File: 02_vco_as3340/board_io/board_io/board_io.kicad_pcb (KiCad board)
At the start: 2 copper layers, 48.8 x 55 mm, 9 parts, among them J1 Conn_02x05_Odd_Even, J2 Conn_02x04_Odd_Even, SW2 SW_SPDT

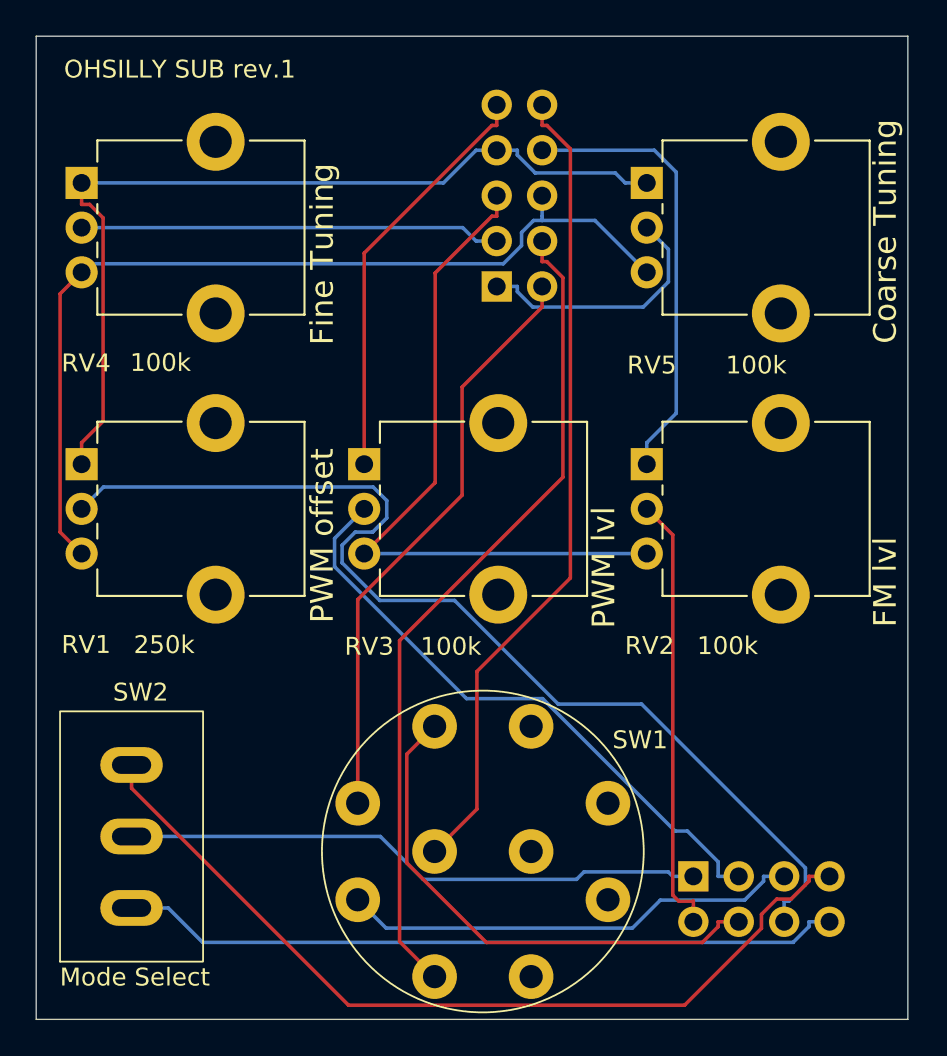
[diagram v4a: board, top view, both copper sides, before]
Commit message: fixed potentiometer direction
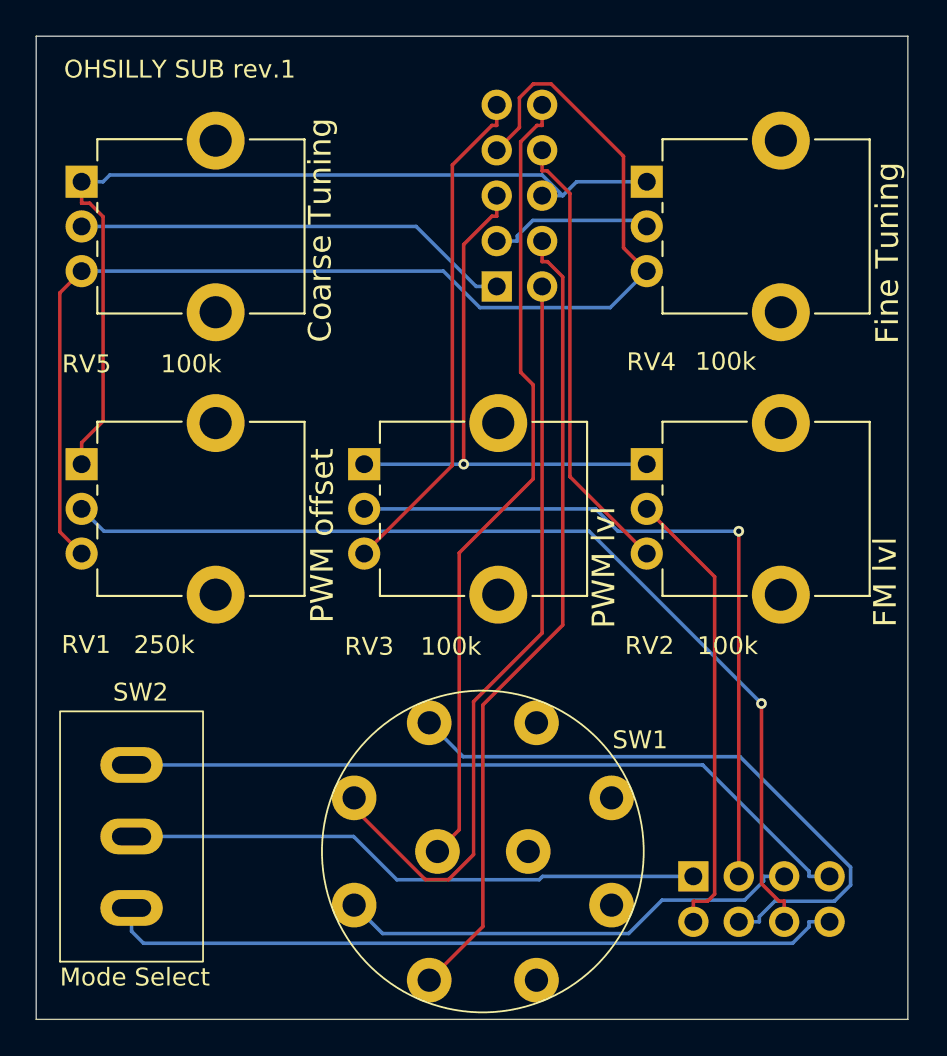
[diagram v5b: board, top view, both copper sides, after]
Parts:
- moved RV4 31.6 mm to (48.8, 26.5)
- moved RV5 31.6 mm to (17.2, 26.5)
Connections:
- RV1 pad 1: +12V -> -12V
- RV1 pad 3: -12V -> +12V
- RV2 pad 1: FM CV Hot -> GND
- RV2 pad 3: GND -> FM CV Hot
- RV3 pad 1: PWM CV Hot -> GND
- RV3 pad 3: GND -> PWM CV Hot
- RV4 pad 1: +12V -> -12V
- RV4 pad 3: -12V -> +12V
- RV5 pad 1: +12V -> -12V
- RV5 pad 3: -12V -> +12V
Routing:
- net +12V: track 50.3 -> 68.4 mm
- net Fine Tuning: track 23.5 -> 9.18 mm
- net Coarse Tuning: track 14.4 -> 24.6 mm
- net Hard Sync -: track 33.2 -> 42.9 mm
- net GND: track 39.1 -> 31.8 mm, vias 0 -> 1
- net Mode VCO: track 49.0 -> 41.8 mm
- net PWM CV Levelled: track 34.2 -> 40.8 mm, vias 0 -> 1
- net Soft Sync: track 29.3 -> 35.2 mm
- net PWM CV Hot: track 23.3 -> 28.3 mm
- net PWM Offset: track 59.6 -> 55.4 mm, vias 0 -> 1
- net -12V: track 52.6 -> 50.8 mm
- net Hard Sync +: track 46.4 -> 45.1 mm
- net FM CV Levelled: track 24.7 -> 25.6 mm
- net Mode LFO: track 40.5 -> 41.3 mm
- net Sync COM: track 45.7 -> 44.9 mm

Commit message: final tweaks
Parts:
- RV1, RV2, RV3, RV4, RV5: footprint Potentiometer_THT:Potentiometer_Alpha_RD901F-40-00D_Single_Vertical_CircularHoles -> cynthia:pot
- moved RV4 7.02 mm to (55.8, 25.8)
- moved RV2 7.01 mm to (55.8, 42.8)
- moved RV3 6.06 mm to (39.1, 42.8)
- moved RV5 5.12 mm to (22.3, 25.8)
- moved RV1 5.11 mm to (22.3, 42.8)
- moved SW2 0.77 mm to (20.8, 63.2)
- moved SW1 0.60 mm to (39.1, 63.9)
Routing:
- net PWM CV Levelled: track 40.8 -> 25.9 mm
- net GND: track 31.8 -> 42.2 mm, vias 1 -> 0
- net Fine Tuning: track 9.18 -> 17.9 mm
- net +12V: track 68.4 -> 60.9 mm, vias 0 -> 1
- net FM CV Hot: track 25.2 -> 31.7 mm
- net PWM Offset: track 55.4 -> 49.7 mm, vias 1 -> 0
- net FM CV Levelled: track 25.6 -> 20.3 mm
- net Coarse Tuning: track 24.6 -> 19.4 mm
- net -12V: track 50.8 -> 55.6 mm
- net Sync COM: track 44.9 -> 49.4 mm
- net Soft Sync: track 35.2 -> 31.6 mm, vias 0 -> 1
- net Hard Sync +: track 45.1 -> 46.5 mm
- net Hard Sync -: track 42.9 -> 41.9 mm, vias 0 -> 1
- net Mode VCO: track 41.8 -> 41.0 mm
- net Mode LFO: track 41.3 -> 40.5 mm
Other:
- board size 48.8 x 55 mm -> 50 x 55 mm
